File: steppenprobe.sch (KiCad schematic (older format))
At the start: 84 parts, among them J1 USB_C_Receptacle_USB2.0, J2 Conn_ST_STDC14, J4 Conn_01x16, Q1 2N7002, SW1 SW_SPDT, SW2 SW_Push, U1 FT2232H, U10 74LVC1G125, U11 74LVC1G125, U12 74LVC1G125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

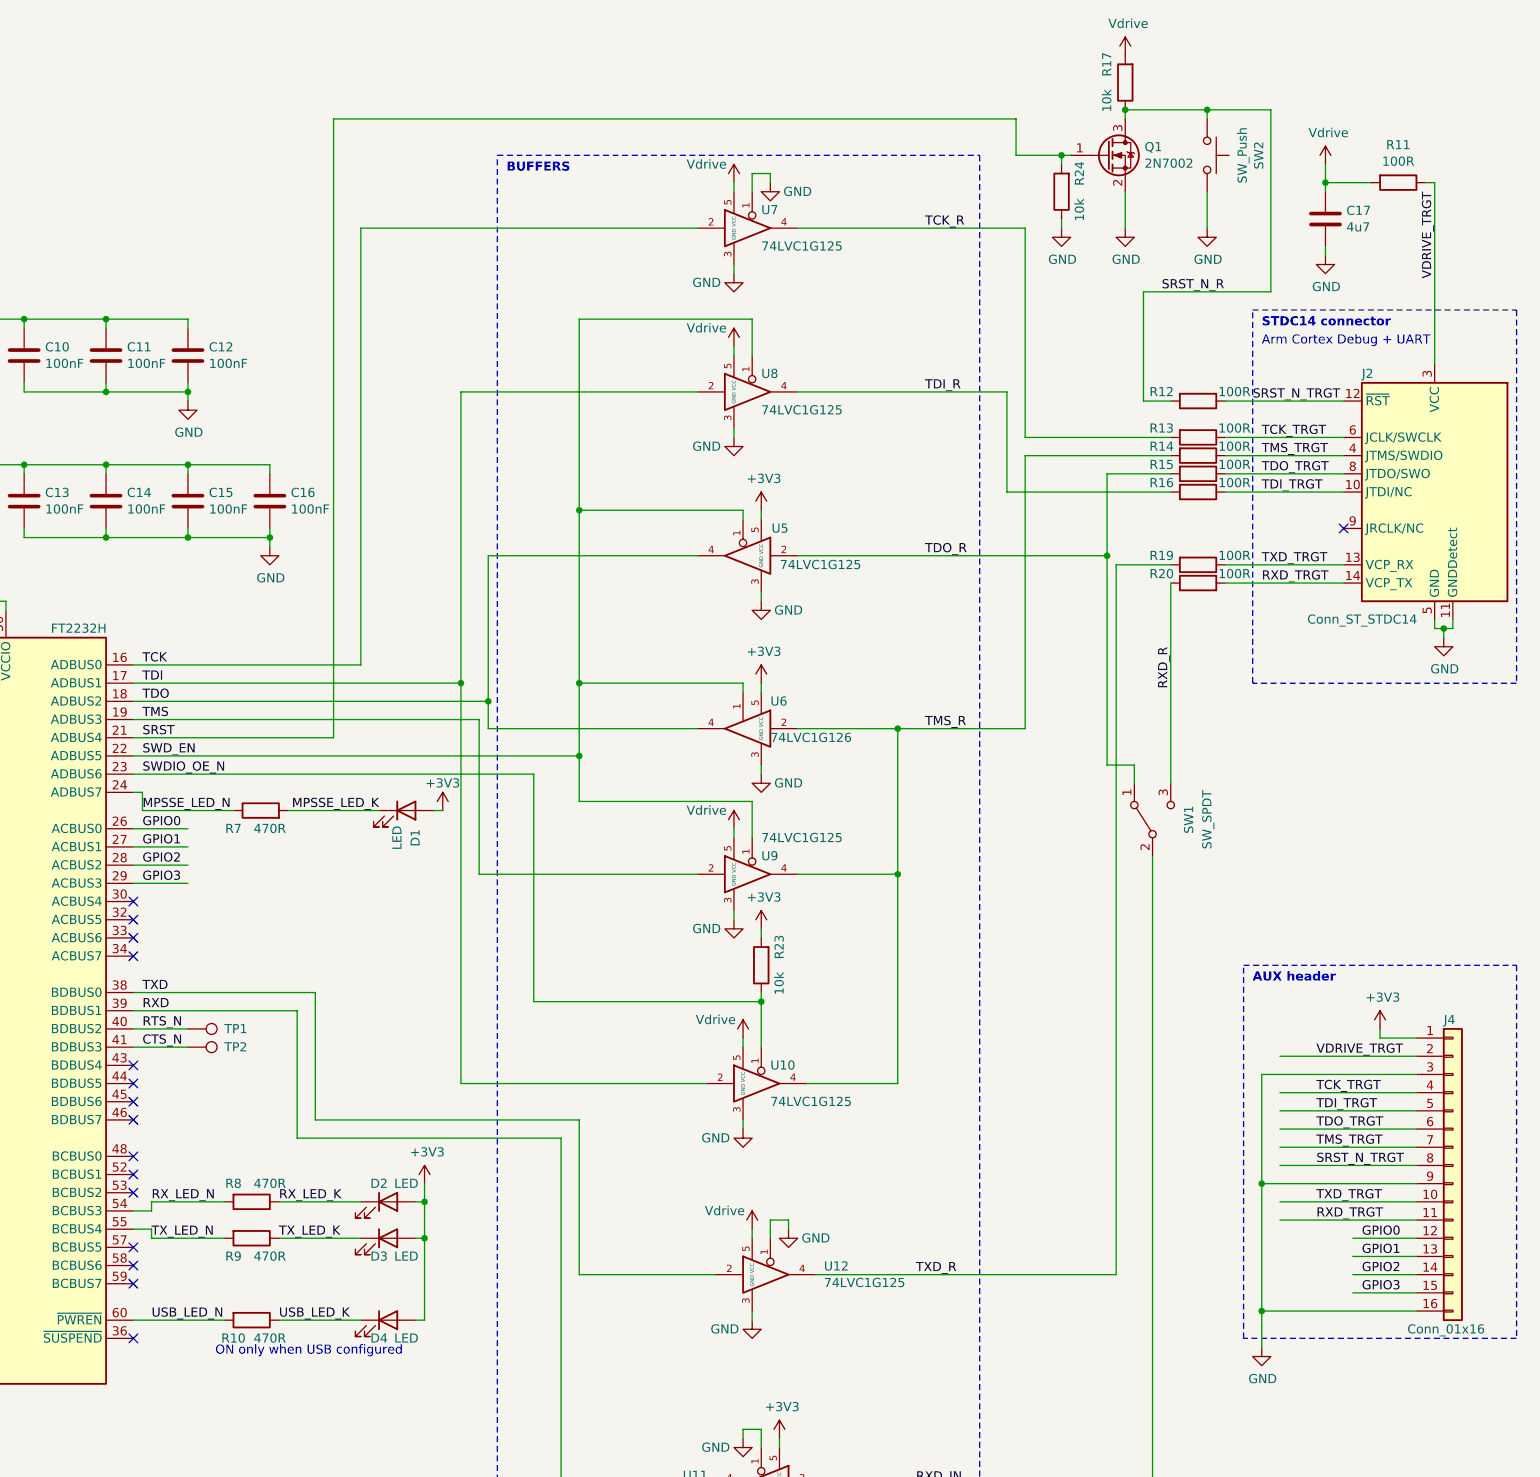
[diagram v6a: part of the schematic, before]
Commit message: Swap activity led and reset output. Remap GPIOs. Plus some tidy up.
- GPIOs only using pins which boot as input (with 75k pull up): GPIO0 was
driven low on boot which can cause undesired effects. GPI03 booted as
RXLED# which is an input with a PU on idle but it could togle low if the
chip receives anything on RX (e.g. noise).
- MPSSE_LED_N renamed as ACT_LED_N (shorter)
- GPIO{0..3} renamed as GPIO_{A-D}: so that they are not confused with
the FTDI numbering.
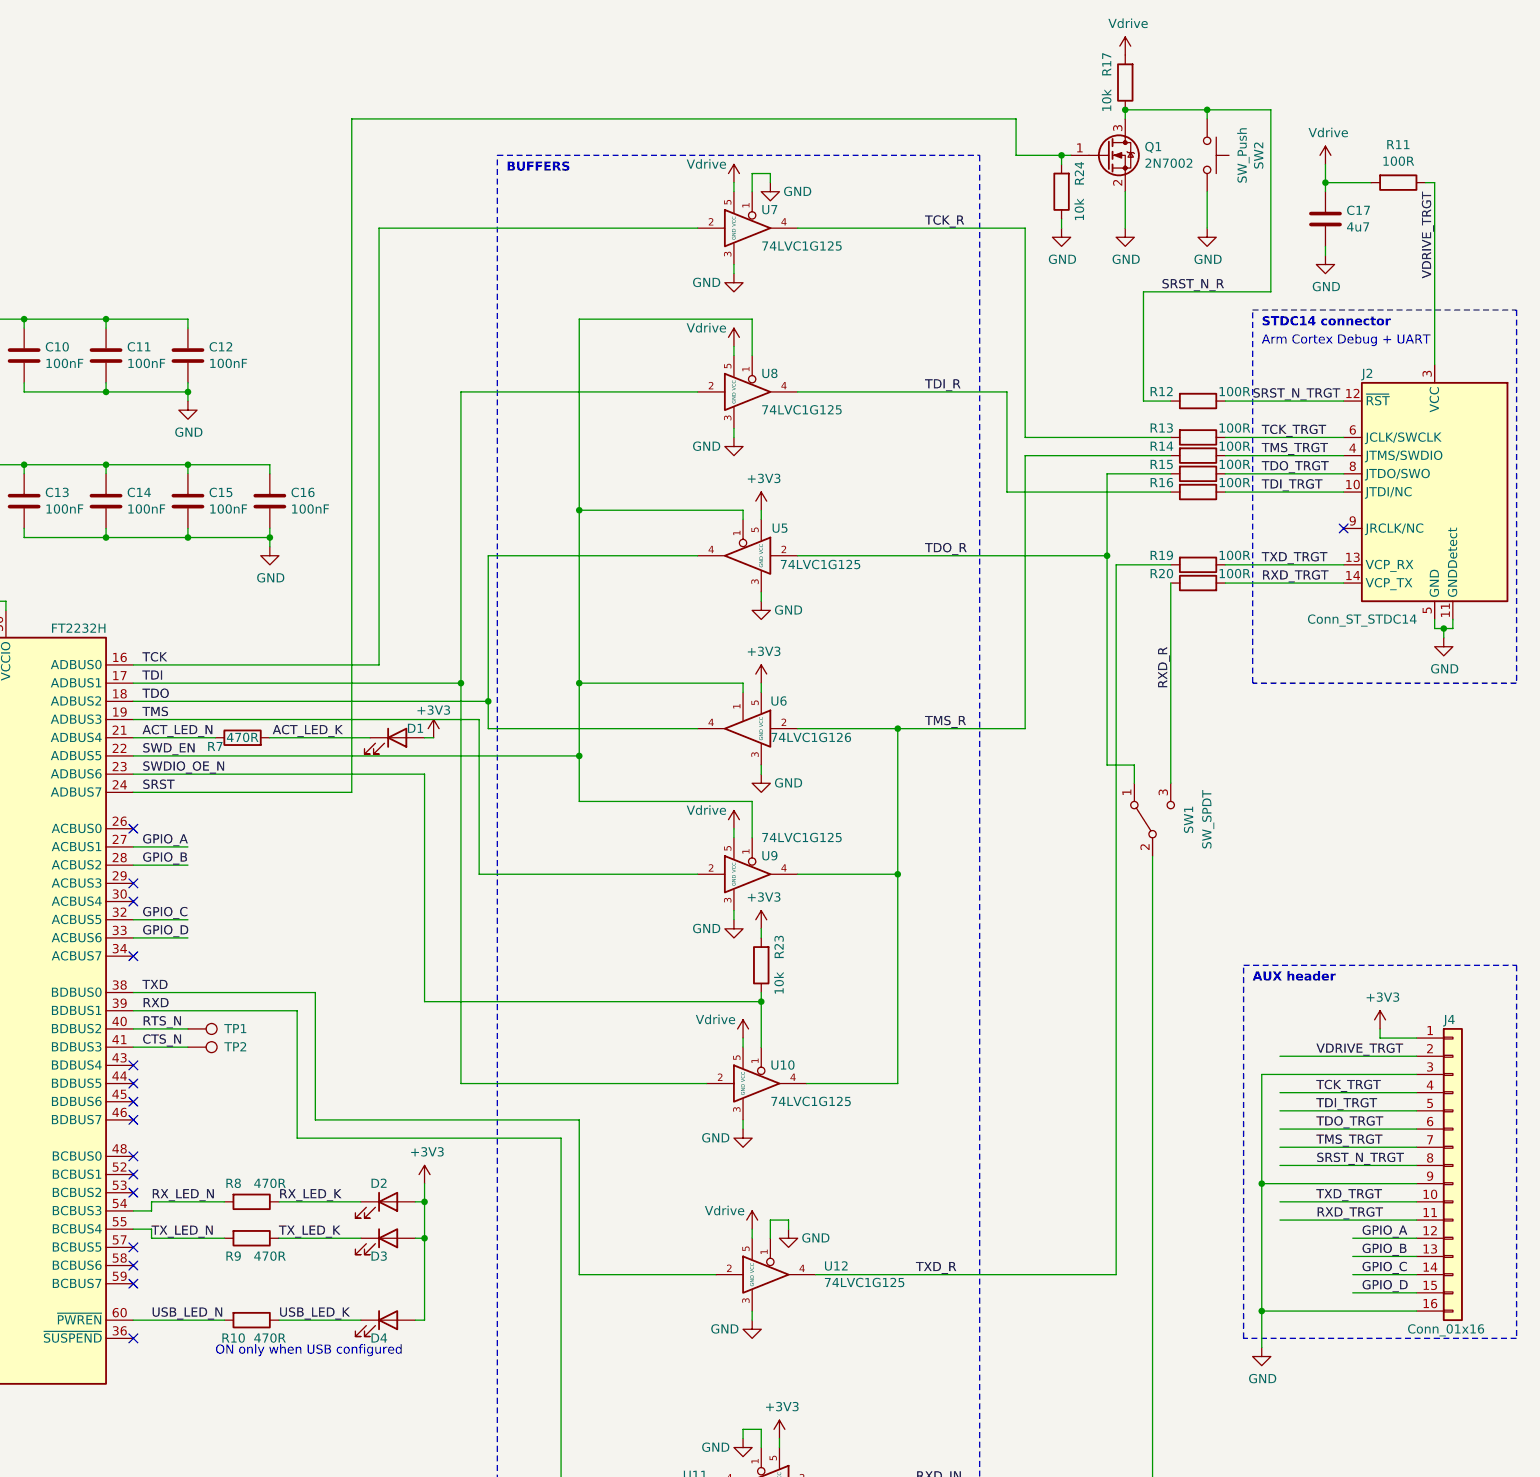
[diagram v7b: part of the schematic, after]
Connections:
- net labels added: ACT_LED_K, ACT_LED_N, GPIO_A, GPIO_B, GPIO_C, GPIO_D
- net labels removed: GPIO0, GPIO1, GPIO2, GPIO3, MPSSE_LED_K, MPSSE_LED_N
- wire segments 372 -> 370
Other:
- moved on the sheet: D1, R7
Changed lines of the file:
@@
 P 9800 7000
 F 0 "D2" H 9750 7100 50  0000 C CNN
-F 1 "LED" H 9900 7100 50  0000 C CNN
+F 1 "LED" H 9900 7100 50  0001 C CNN
 F 2 "LED_SMD:LED_0603_1608Metric" H 9800 7000 50  0001 C CNN
 F 3 "~" H 9800 7000 50  0001 C CNN
@@
 P 9800 7200
 F 0 "D3" H 9750 7100 50  0000 C CNN
-F 1 "LED" H 9900 7100 50  0000 C CNN
+F 1 "LED" H 9900 7100 50  0001 C CNN
 F 2 "LED_SMD:LED_0603_1608Metric" H 9800 7200 50  0001 C CNN
 F 3 "~" H 9800 7200 50  0001 C CNN
@@
 	1    0    0    -1
 $EndComp
-Text Label 8450 4050 0    50   ~ 0
-TCK
-Text Label 8450 4150 0    50   ~ 0
-TDI
-Text Label 8450 4250 0    50   ~ 0
-TDO
-Text Label 8450 4350 0    50   ~ 0
-TMS
-Text Label 8450 4450 0    50   ~ 0
-SRST
 Text Label 8450 5850 0    50   ~ 0
 TXD
@@
 P 9800 7650
 F 0 "D4" H 9750 7550 50  0000 C CNN
-F 1 "LED" H 9900 7550 50  0000 C CNN
+F 1 "LED" H 9900 7550 50  0001 C CNN
 F 2 "LED_SMD:LED_0603_1608Metric" H 9800 7650 50  0001 C CNN
 F 3 "~" H 9800 7650 50  0001 C CNN
@@
 ON only when USB configured
 Wire Wire Line
-	9650 4050 9650 1650
-Wire Wire Line
-	8400 4050 9650 4050
-Text Label 8450 4550 0    50   ~ 0
-SWD_EN
-Text Label 8450 4650 0    50   ~ 0
-SWDIO_OE_N
+	9750 4050 9750 1650
+Wire Wire Line
+	8400 4050 9750 4050
 Wire Wire Line
 	8400 4150 10200 4150
@@
 Connection ~ 10200 4150
 Wire Wire Line
-	8400 4650 10600 4650
+	8400 4650 10000 4650
 NoConn ~ 8400 7450
 NoConn ~ 8400 7350
@@
 NoConn ~ 8400 6250
 NoConn ~ 8400 5650
-NoConn ~ 8400 5550
-NoConn ~ 8400 5450
+NoConn ~ 8400 5250
 NoConn ~ 8400 5350
+NoConn ~ 8400 4950
 NoConn ~ 8400 7750
 $Comp
@@
 	1    0    0    -1
 $EndComp
-Wire Wire Line
-	8400 4450 9500 4450
 Wire Notes Line
 	2950 6100 2950 7500
@@
 $EndComp
 Wire Wire Line
-	9650 1650 11500 1650
+	9750 1650 11500 1650
 Wire Wire Line
 	10200 2550 11500 2550
@@
 	10200 6350 11550 6350
 Wire Wire Line
-	10600 4650 10600 5900
+	10000 4650 10000 5900
 Wire Wire Line
 	10350 3450 11500 3450
@@
 Wire Wire Line
 	15450 6700 14700 6700
-Text Label 8450 5250 0    50   ~ 0
-GPIO3
-Text Label 8450 5150 0    50   ~ 0
-GPIO2
-Text Label 8450 5050 0    50   ~ 0
-GPIO1
-Text Label 8450 4950 0    50   ~ 0
-GPIO0
-Wire Wire Line
-	8400 4950 8700 4950
+Text Label 8450 5450 0    50   ~ 0
+GPIO_C
+Wire Wire Line
+	8400 5450 8700 5450
 Wire Wire Line
 	8400 5050 8700 5050
 Wire Wire Line
 	8400 5150 8700 5150
-Wire Wire Line
-	8400 5250 8700 5250
 Text Label 15150 7500 0    50   ~ 0
-GPIO3
+GPIO_D
 Wire Wire Line
 	15450 7200 15100 7200
@@
 	15450 7500 15100 7500
 Text Label 15150 7400 0    50   ~ 0
-GPIO2
+GPIO_C
 Text Label 15150 7300 0    50   ~ 0
-GPIO1
+GPIO_B
 Text Label 15150 7200 0    50   ~ 0
-GPIO0
+GPIO_A
 $Comp
 L Device:Crystal_GND24 Y1
@@
 $EndComp
 $Comp
-L Interface_USB:FT2232H U1
-U 1 1 5C60DA40
-P 7200 5950
-F 0 "U1" H 6200 8050 50  0000 C CNN
-F 1 "FT2232H" H 8100 8050 50  0000 C CNN
-F 2 "Package_QFP:LQFP-64_10x10mm_P0.5mm" H 7200 5950 50  0001 C CNN
-F 3 "http://www.ftdichip.com/Products/ICs/FT2232H.html" H 7200 5950 50  0001 C CNN
-F 4 "FTDI" H 7200 5950 50  0001 C CNN "Manufacturer"
-F 5 "FT2232HL" H 7200 5950 50  0001 C CNN "MPN"
-F 6 "C27882" H 7200 5950 50  0001 C CNN "LCSC_PN"
-	1    7200 5950
-	1    0    0    -1
-$EndComp
-$Comp
 L Device:C C22
 U 1 1 5DB8298F
@@
 Wire Wire Line
 	11500 4400 10350 4400
-Text Label 8450 4850 0    50   ~ 0
-MPSSE_LED_N
-Wire Wire Line
-	8400 4750 8450 4750
-Wire Wire Line
-	8450 4850 8450 4750
-$Comp
-L Device:R R7
-U 1 1 5C62F38F
-P 9100 4850
-F 0 "R7" V 9000 5000 50  0000 C CNN
-F 1 "470R" V 9000 4800 50  0000 C CNN
-F 2 "Resistor_SMD:R_0603_1608Metric" V 9030 4850 50  0001 C CNN
-F 3 "~" H 9100 4850 50  0001 C CNN
-F 4 "C23179" H 9100 4850 50  0001 C CNN "LCSC_PN"
-	1    9100 4850
-	0    -1   -1   0
-$EndComp
-Wire Wire Line
-	8950 4850 8450 4850
-$Comp
-L Device:LED D1
-U 1 1 5C62F385
-P 9900 4850
-F 0 "D1" V 9950 4700 50  0000 C CNN
-F 1 "LED" V 9850 4700 50  0000 C CNN
-F 2 "LED_SMD:LED_0603_1608Metric" H 9900 4850 50  0001 C CNN
-F 3 "~" H 9900 4850 50  0001 C CNN
-F 4 "C72043" H 9900 4850 50  0001 C CNN "LCSC_PN"
-F 5 "19-217/GHC-YR1S2/3T" H 9900 4850 50  0001 C CNN "MPN"
-F 6 "Everlight Elec" H 9900 4850 50  0001 C CNN "Manufacturer"
-F 7 "150060GS75000" H 9900 4850 50  0001 C CNN "MPN2"
-F 8 "Wurth Electronic" H 9900 4850 50  0001 C CNN "Manufacturer2"
-	1    9900 4850
-	1    0    0    -1
-$EndComp
-$Comp
-L power:+3V3 #PWR0108
-U 1 1 5DBB9689
-P 10100 4850
-F 0 "#PWR0108" H 10100 4700 50  0001 C CNN
-F 1 "+3V3" H 10100 5000 50  0000 C CNN
-F 2 "" H 10100 4850 50  0001 C CNN
-F 3 "" H 10100 4850 50  0001 C CNN
-	1    10100 4850
-	1    0    0    -1
-$EndComp
-Wire Wire Line
-	10050 4850 10100 4850
+Wire Wire Line
+	10000 4450 10050 4450
 $Comp
 L Device:R R23
@@
 Wire Wire Line
 	14100 2600 13950 2600
-Wire Wire Line
-	9500 4450 9500 1050
-Wire Wire Line
-	9500 1050 13250 1050
 $Comp
 L power:GND #PWR066
@@
 	13550 1250 13500 1250
 Wire Wire Line
-	13250 1250 13250 1050
-Wire Wire Line
 	13500 1300 13500 1250
 Connection ~ 13500 1250
 Wire Wire Line
 	13500 1250 13250 1250
-Text Label 9750 4850 2    50   ~ 0
-MPSSE_LED_K
-Wire Wire Line
-	9250 4850 9750 4850
 Wire Wire Line
 	13300 2900 14100 2900
@@
 Connection ~ 11850 5900
 Wire Wire Line
-	10600 5900 11850 5900
+	10000 5900 11850 5900
+$Comp
+L power:+3V3 #PWR0108
+U 1 1 5DBB9689
+P 10050 4450
+F 0 "#PWR0108" H 10050 4300 50  0001 C CNN
+F 1 "+3V3" H 10050 4600 50  0000 C CNN
+F 2 "" H 10050 4450 50  0001 C CNN
+F 3 "" H 10050 4450 50  0001 C CNN
+	1    10050 4450
+	1    0    0    -1
+$EndComp
+$Comp
+L Device:LED D1
+U 1 1 5C62F385
+P 9850 4450
+F 0 "D1" H 9950 4500 50  0000 C CNN
+F 1 "LED" H 10000 4400 50  0001 C CNN
+F 2 "LED_SMD:LED_0603_1608Metric" H 9850 4450 50  0001 C CNN
+F 3 "~" H 9850 4450 50  0001 C CNN
+F 4 "C72043" H 9850 4450 50  0001 C CNN "LCSC_PN"
+F 5 "19-217/GHC-YR1S2/3T" H 9850 4450 50  0001 C CNN "MPN"
+F 6 "Everlight Elec" H 9850 4450 50  0001 C CNN "Manufacturer"
+F 7 "150060GS75000" H 9850 4450 50  0001 C CNN "MPN2"
+F 8 "Wurth Electronic" H 9850 4450 50  0001 C CNN "Manufacturer2"
+	1    9850 4450
+	1    0    0    -1
+$EndComp
+Wire Wire Line
+	8850 4450 8400 4450
+Text Label 8450 4450 0    50   ~ 0
+ACT_LED_N
+Text Label 9550 4450 2    50   ~ 0
+ACT_LED_K
+$Comp
+L Device:R R7
+U 1 1 5C62F38F
+P 9000 4450
+F 0 "R7" V 8950 4600 50  0000 C CNN
+F 1 "470R" V 9000 4450 50  0000 C CNN
+F 2 "Resistor_SMD:R_0603_1608Metric" V 8930 4450 50  0001 C CNN
+F 3 "~" H 9000 4450 50  0001 C CNN
+F 4 "C23179" H 9000 4450 50  0001 C CNN "LCSC_PN"
+	1    9000 4450
+	0    -1   -1   0
+$EndComp
+Text Label 8450 4050 0    50   ~ 0
+TCK
+Text Label 8450 4150 0    50   ~ 0
+TDI
+Text Label 8450 4250 0    50   ~ 0
+TDO
+Text Label 8450 4350 0    50   ~ 0
+TMS
+Text Label 8450 4650 0    50   ~ 0
+SWDIO_OE_N
+Text Label 8450 4550 0    50   ~ 0
+SWD_EN
+Wire Wire Line
+	9150 4450 9700 4450
+Wire Wire Line
+	9600 1050 9600 4750
+Wire Wire Line
+	8400 4750 9600 4750
+Wire Wire Line
+	13250 1250 13250 1050
+Wire Wire Line
+	9600 1050 13250 1050
+Text Label 8450 4750 0    50   ~ 0
+SRST
+Text Label 8450 5150 0    50   ~ 0
+GPIO_B
+Text Label 8450 5050 0    50   ~ 0
+GPIO_A
+$Comp
+L Interface_USB:FT2232H U1
+U 1 1 5C60DA40
+P 7200 5950
+F 0 "U1" H 6200 8050 50  0000 C CNN
+F 1 "FT2232H" H 8100 8050 50  0000 C CNN
+F 2 "Package_QFP:LQFP-64_10x10mm_P0.5mm" H 7200 5950 50  0001 C CNN
+F 3 "http://www.ftdichip.com/Products/ICs/FT2232H.html" H 7200 5950 50  0001 C CNN
+F 4 "FTDI" H 7200 5950 50  0001 C CNN "Manufacturer"
+F 5 "FT2232HL" H 7200 5950 50  0001 C CNN "MPN"
+F 6 "C27882" H 7200 5950 50  0001 C CNN "LCSC_PN"
+	1    7200 5950
+	1    0    0    -1
+$EndComp
+Wire Wire Line
+	8400 5550 8700 5550
+Text Label 8450 5550 0    50   ~ 0
+GPIO_D
 $EndSCHEMATC

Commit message: Replace reset switch and layout changes
- Reset switch SW_Push_1P1T_NO_E-Switch_TL3301NxxxxxG instead of SW_SPST_PTS645.
  The old one is smaller and not compatible (or at least too tight) with many easily sourceable 6mm switches.
  The new footprint should be compatible with many more options including the previous PTS645.
  Some small tweaks were required around it given its slightly bigger size.
- Version now v1.0
- GPIO names changed from 0-3 to A-D
- FTDI channel note made bigger and thicker. Now vertical left of the QR.
- QR not inverted anymore (some scanners struggled to read it).
- WEEE symbol added and symbols placed at the south end on the bottom side.
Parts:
- SW2: footprint Button_Switch_SMD:SW_SPST_PTS645 -> Button_Switch_SMD:SW_Push_1P1T_NO_E-Switch_TL3301NxxxxxG
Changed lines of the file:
@@
 Title "Steppenprobe"
 Date ""
-Rev "v0.1"
+Rev "v1.0"
 Comp "Diego Herranz"
 Comment1 ""
 Comment2 ""
-Comment3 ""
-Comment4 ""
+Comment3 "Debugging and boundary scan"
+Comment4 "JTAG/SWD and UART/SWO USB interface board"
 Comment5 ""
 Comment6 ""
@@
 F 0 "SW2" H 14300 1535 50  0000 C CNN
 F 1 "SW_Push" H 14300 1444 50  0000 C CNN
-F 2 "Button_Switch_SMD:SW_SPST_PTS645" H 14300 1450 50  0001 C CNN
+F 2 "Button_Switch_SMD:SW_Push_1P1T_NO_E-Switch_TL3301NxxxxxG" H 14300 1450 50  0001 C CNN
 F 3 "~" H 14300 1450 50  0001 C CNN
 F 4 "PTS645SK43SMTR92 LFS" H 14300 1250 50  0001 C CNN "MPN"
